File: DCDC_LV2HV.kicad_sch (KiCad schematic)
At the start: 9 parts

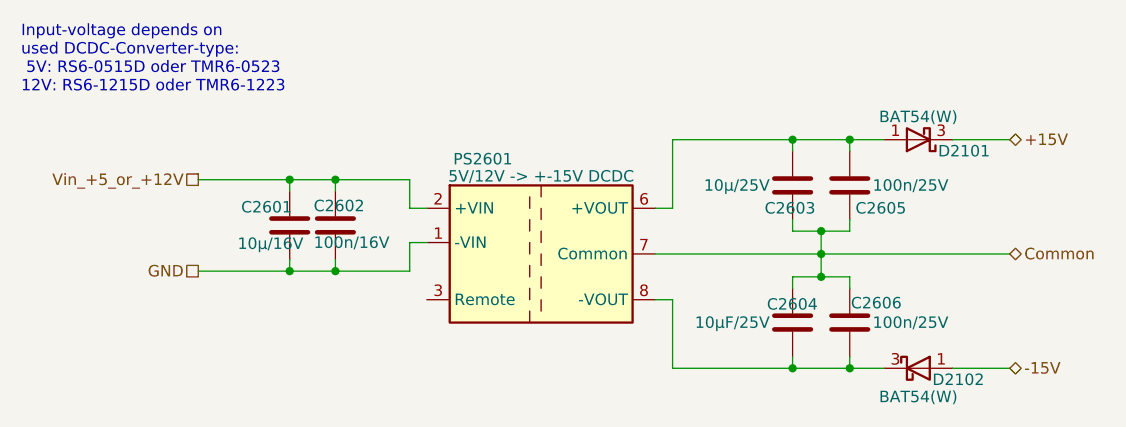
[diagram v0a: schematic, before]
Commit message: FEAR-16 V2.2
PCB-Changes:
 - Added rudimentary "load-balancer" (not really a balancer, but should avoid the DC/DC from regulating against each other!)
 - Added optional GND-jumpers to the N/C pins of the shields
 - Modified amplification adjustment:
   -> Added a offset resistor in row to the trim-poti for amplification for finer amp-tuning
   -> Reduced trim-poti-value from 1Meg -> 50k (20x finer adjustment-range)
      Poti can in the range of:
      - 30k (min) for being able to reach the correct amplification
      - 50k (max) for having at least 20x finer tune-range and a bit of reserve, as 30k is pretty thight on tolerance

Misc.:
 - Added LICENSE.md
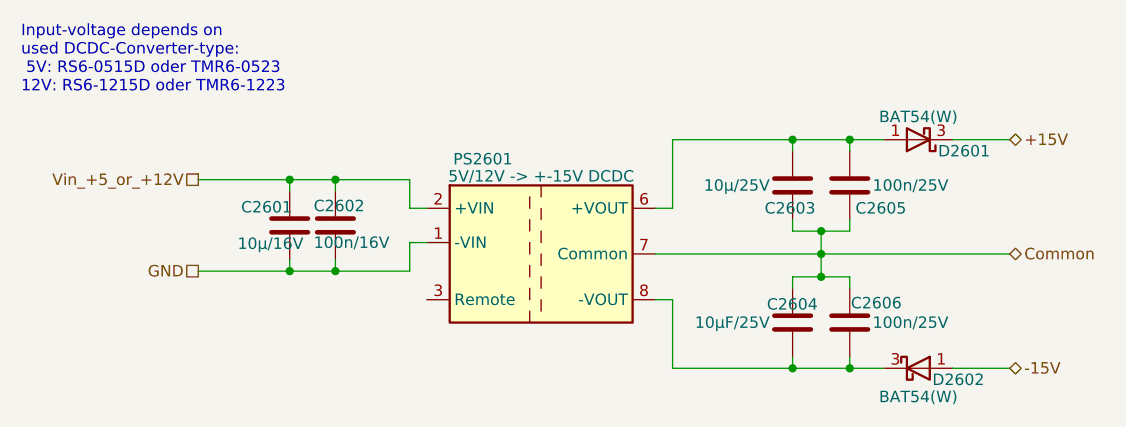
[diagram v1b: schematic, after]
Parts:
- renumbered D2101 to D2601, D2102 to D2602

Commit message: Fixed ADP2370 designator
ADP2370 has a bunch of fixed output voltages and an adjustable model.
We use the adjustable model, so we fixed the name matching with the correct model-name.
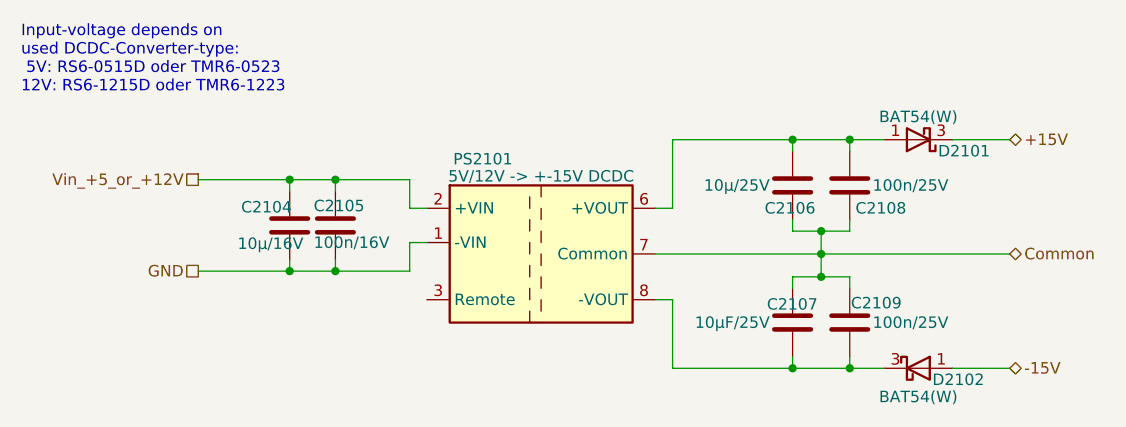
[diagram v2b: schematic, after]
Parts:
- renumbered C2601 to C2104, C2602 to C2105, C2603 to C2106, C2604 to C2107, C2605 to C2108, C2606 to C2109, D2601 to D2101, D2602 to D2102, PS2601 to PS2101
